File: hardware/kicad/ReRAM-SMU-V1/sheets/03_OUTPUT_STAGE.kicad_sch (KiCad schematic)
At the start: 21 parts, among them U301 LT1970AIFE#PBF TSSOP-20 EP

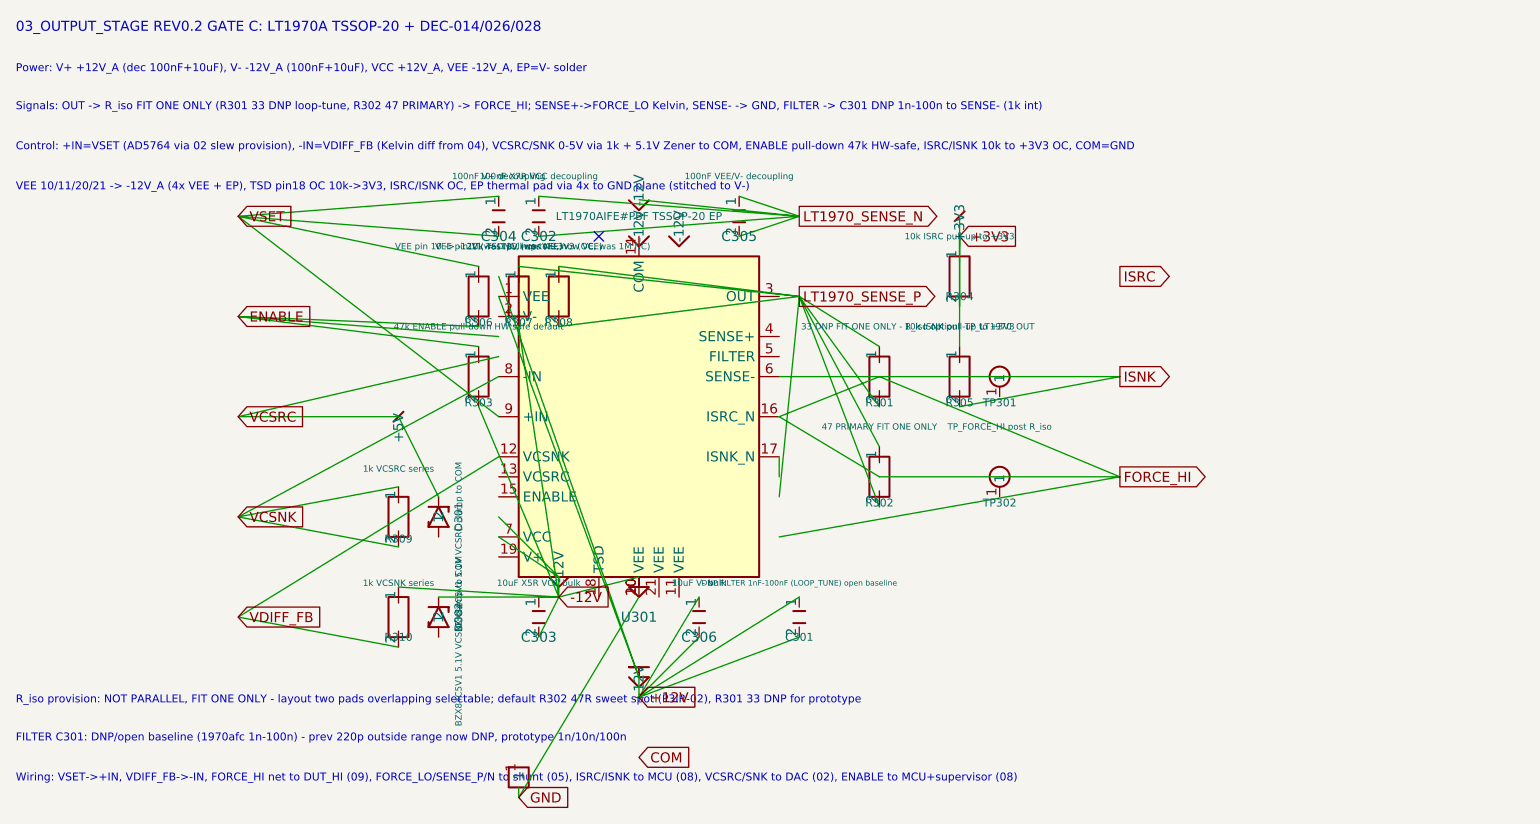
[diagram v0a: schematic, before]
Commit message: style(kicad): re-serialize 01-06 + root to KiCad 9.0 schema 20250114 (formatting only)
- (version 20241014)->(version 20250114) + generator_version 10.0->9.0 on all 10 sch files including root + 01-04 verified via git diff
- lib_symbols block pretty-print expansion: property/symbol multi-line with explicit hide/exclude/effects font, no wire/symbol/net deletion
- 8 files: ReRAM-SMU-V1.kicad_pro (453+9-), ReRAM-SMU-V1.kicad_sch (806+53-), 01_POWER (5724+411-), 02_DAC (5816+436-), 03_OUTPUT (4308+276-), 04_KELVIN (3720+270-), 05_CURRENT_RANGES (375+217-), 06_ADC (492+452-); total 21694+2124-
- 07/08/09 excluded (already restored 184/236/156 lines, verified not truncated; no re-serialization needed)
- Functional audit: no net/junction/wire loss, netlist continuity preserved, ERC 124 headless (ca7eac3) unchanged by re-serialization
- Verified: wc -l 01 5739,02 5831,03 4322,04 3735,05 388,06 507,07 184,08 236,09 156
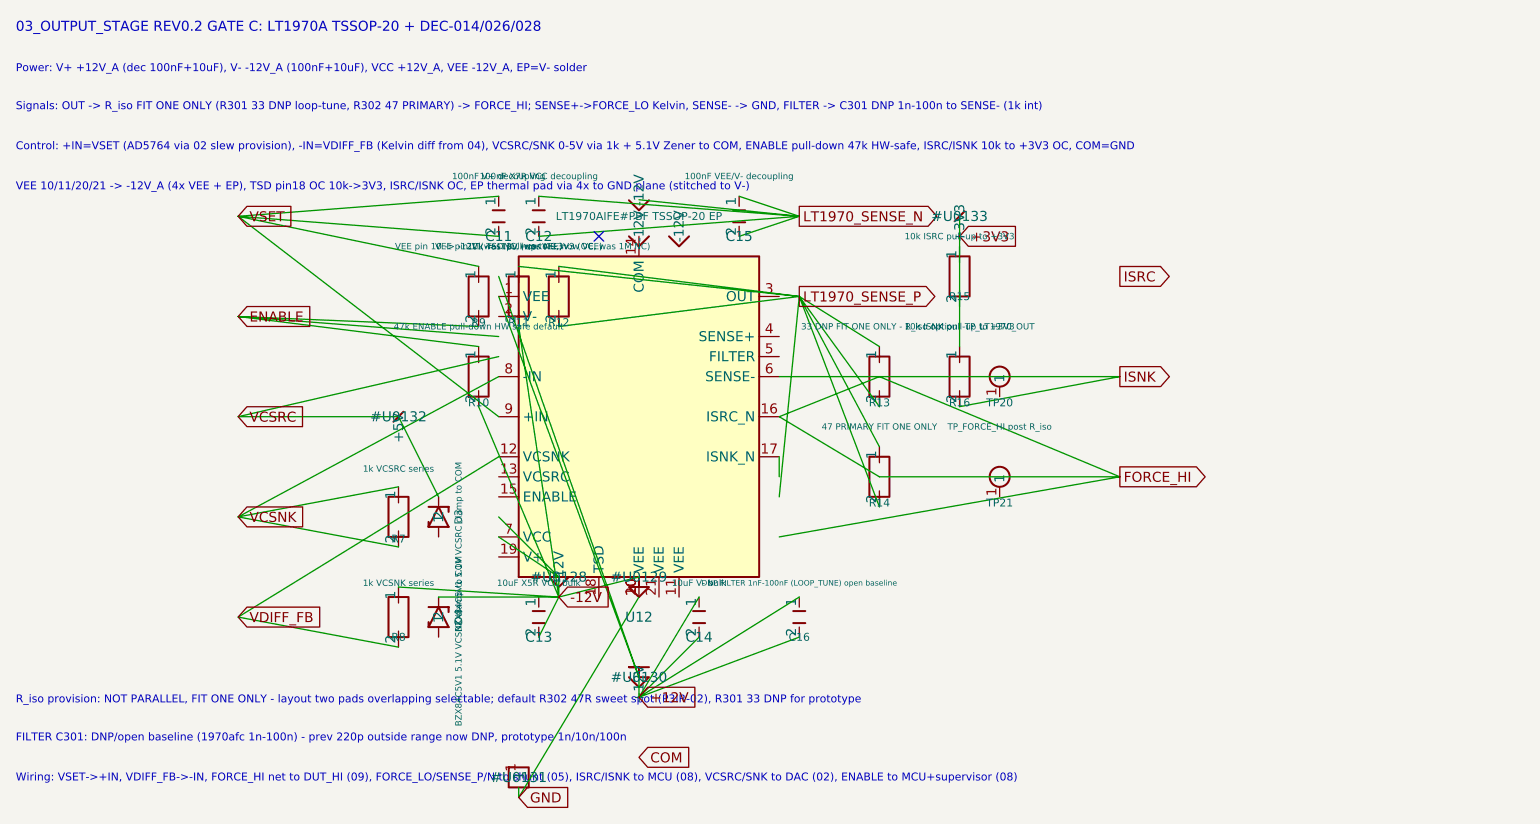
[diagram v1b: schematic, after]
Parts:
- renumbered C304 to C11, C302 to C12, C303 to C13, C306 to C14, C305 to C15, C301 to C16, D301 to D3, D302 to D4, R303 to R10, R307 to R11, R308 to R12, R301 to R13, R302 to R14, R304 to R15, R305 to R16, R309 to R7, R310 to R8, R306 to R9, TP301 to TP20, TP302 to TP21, U301 to U12
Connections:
- net +3V3: no longer R15.1, R15.2
- net -12V: no longer C13.1
